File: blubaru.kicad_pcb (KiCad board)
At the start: 2 copper layers, 97.8 x 94.6 mm, 38 parts, among them J1 DB15, J2 DB15, J3 FSA2269, J4 ProMicro, J5 RN52_BREAKOUT, J6 JACK_TRS_6PINS, J7 TPA6112, P1 CONN_01X06, U1 DG419

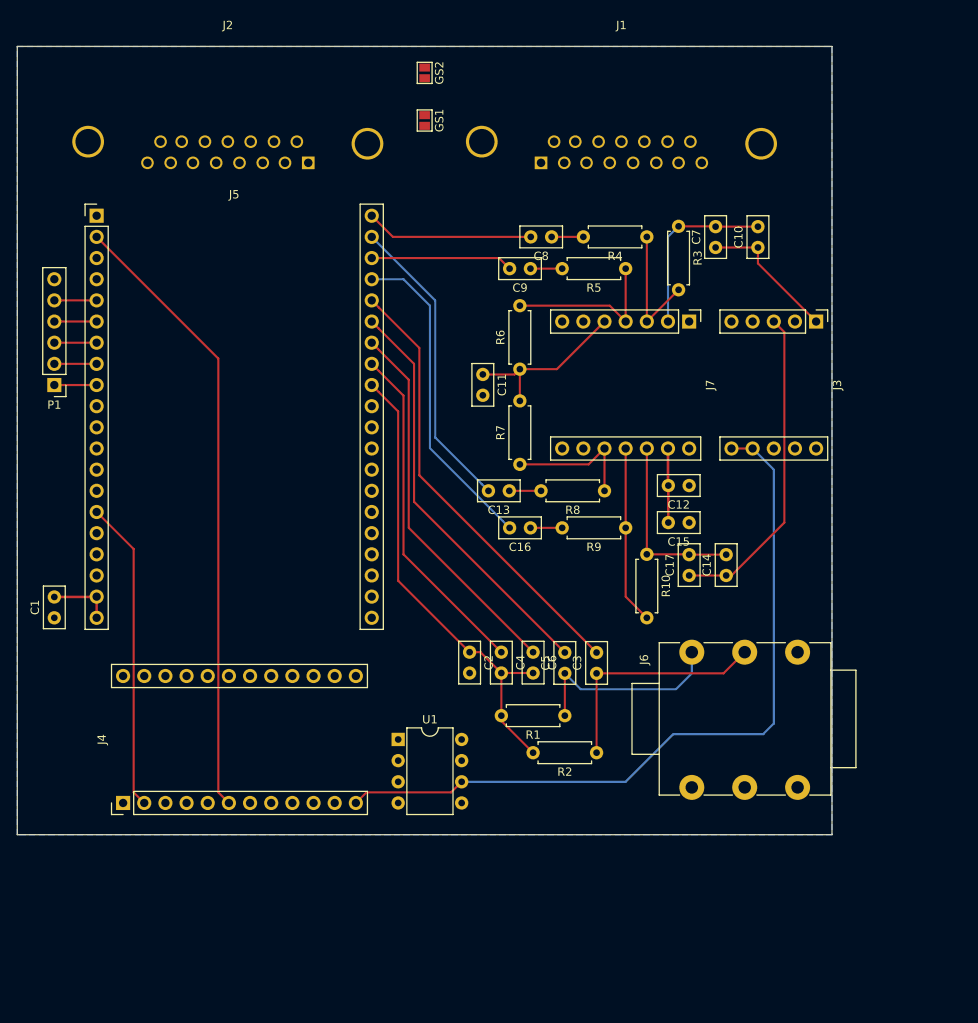
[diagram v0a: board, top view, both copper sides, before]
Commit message: Add footprints for LEDs and tactile switches
Also create an initial layout for fun.
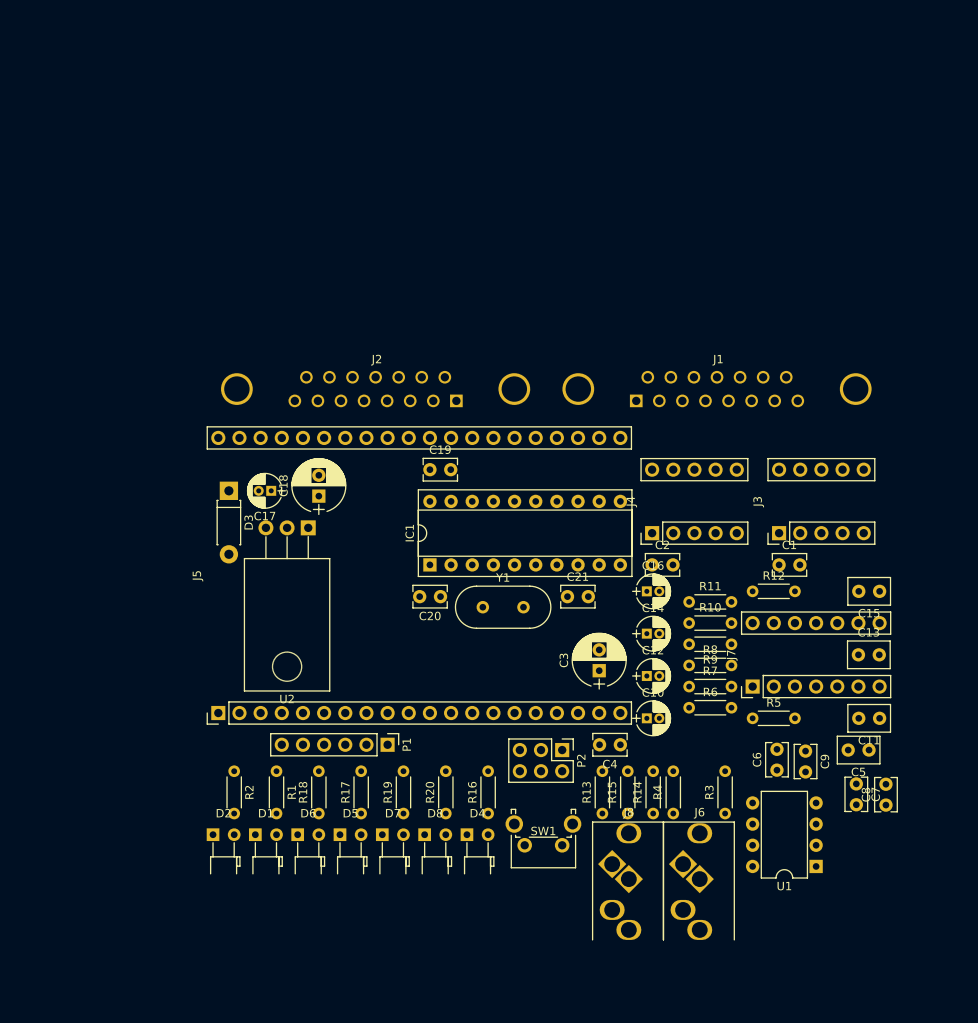
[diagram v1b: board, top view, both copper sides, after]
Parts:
- removed GS1, GS2: GS2, Connectors:GS2
- added C18: 100uF, blubaru:CP_Radial_D6.3mm_P2.50mm, F.Cu at (120.7, 83.8)
- added C19: 0.1uF, blubaru:C_Disc_D4.0mm_W2.6mm_P2.50mm, F.Cu at (134.0, 80.6)
- added C20: 22pF, blubaru:C_Disc_D4.0mm_W2.6mm_P2.50mm, F.Cu at (135.3, 95.9)
- added C21: 22pF, blubaru:C_Disc_D4.0mm_W2.6mm_P2.50mm, F.Cu at (150.5, 95.9)
- added D1: B LED, blubaru:LED_D3.0mm_Horizontal_O1.27mm_Z6.0mm, F.Cu at (113.0, 124.5)
- added D2: R LED, blubaru:LED_D3.0mm_Horizontal_O1.27mm_Z6.0mm, F.Cu at (108.0, 124.5)
- added D3: D, Diodes_THT:D_DO-41_SOD81_P7.62mm_Horizontal, F.Cu at (109.9, 83.2)
- added D4: R LED, blubaru:LED_D3.0mm_Horizontal_O1.27mm_Z6.0mm, F.Cu at (138.4, 124.5)
- added D5: O LED, blubaru:LED_D3.0mm_Horizontal_O1.27mm_Z6.0mm, F.Cu at (123.2, 124.5)
- added D6: Y LED, blubaru:LED_D3.0mm_Horizontal_O1.27mm_Z6.0mm, F.Cu at (118.1, 124.5)
- added D7: G LED, blubaru:LED_D3.0mm_Horizontal_O1.27mm_Z6.0mm, F.Cu at (128.3, 124.5)
- added D8: B LED, blubaru:LED_D3.0mm_Horizontal_O1.27mm_Z6.0mm, F.Cu at (133.3, 124.5)
- added IC1: ATTINY4313-P, Housings_DIP:DIP-20_W7.62mm_Socket, F.Cu at (134.0, 92.1)
- added J8: JACK_TRS_5PINS, blubaru:sj1-353xng, F.Cu at (157.9, 135.9)
- added P2: CONN_02X03, Pin_Headers:Pin_Header_Straight_2x03_Pitch2.54mm, F.Cu at (149.9, 114.3)
- added R11: 11k, Resistors_THT:R_Axial_DIN0204_L3.6mm_D1.6mm_P5.08mm_Horizontal, F.Cu at (165.1, 96.5)
- added R12: 8.2k, Resistors_THT:R_Axial_DIN0204_L3.6mm_D1.6mm_P5.08mm_Horizontal, F.Cu at (172.7, 95.2)
- added R13: 100k, Resistors_THT:R_Axial_DIN0204_L3.6mm_D1.6mm_P5.08mm_Horizontal, F.Cu at (154.7, 121.9)
- added R14: 100k, Resistors_THT:R_Axial_DIN0204_L3.6mm_D1.6mm_P5.08mm_Horizontal, F.Cu at (160.8, 121.9)
- added R15: 1M, Resistors_THT:R_Axial_DIN0204_L3.6mm_D1.6mm_P5.08mm_Horizontal, F.Cu at (157.7, 121.9)
- added R16: 750, Resistors_THT:R_Axial_DIN0204_L3.6mm_D1.6mm_P5.08mm_Horizontal, F.Cu at (141.0, 121.9)
- added R17: 750, Resistors_THT:R_Axial_DIN0204_L3.6mm_D1.6mm_P5.08mm_Horizontal, F.Cu at (125.7, 121.9)
- added R18: 750, Resistors_THT:R_Axial_DIN0204_L3.6mm_D1.6mm_P5.08mm_Horizontal, F.Cu at (120.7, 121.9)
- added R19: 330, Resistors_THT:R_Axial_DIN0204_L3.6mm_D1.6mm_P5.08mm_Horizontal, F.Cu at (130.8, 121.9)
- added R20: 330, Resistors_THT:R_Axial_DIN0204_L3.6mm_D1.6mm_P5.08mm_Horizontal, F.Cu at (135.9, 121.9)
- added SW1: SW_Push, blubaru:SW_Tactile_SPST_Angled_PTS645Vx58-2LFS, F.Cu at (149.9, 125.7)
- added U2: LD1117V33, TO_SOT_Packages_THT:TO-220_Horizontal, F.Cu at (119.4, 87.6)
- added Y1: 11.0592MHz, Crystals:Crystal_HC49-4H_Vertical, F.Cu at (140.3, 97.2)
- C1: footprint Capacitors_THT:C_Disc_D5.0mm_W2.5mm_P2.50mm -> blubaru:C_Disc_D4.0mm_W2.6mm_P2.50mm
- C10, C14: value 100uF -> 1uF; footprint Capacitors_THT:C_Disc_D5.0mm_W2.5mm_P2.50mm -> blubaru:CP_Radial_D4.0mm_P1.50mm
- C11, C13: footprint Capacitors_THT:C_Disc_D5.0mm_W2.5mm_P2.50mm -> blubaru:C_Disc_D5.0mm_W3.2mm_P2.50mm
- C12: value 0.1uF -> 1uF; footprint Capacitors_THT:C_Disc_D5.0mm_W2.5mm_P2.50mm -> blubaru:CP_Radial_D4.0mm_P1.50mm
- C15: value 10uF -> 1uF; footprint Capacitors_THT:C_Disc_D5.0mm_W2.5mm_P2.50mm -> blubaru:C_Disc_D5.0mm_W3.2mm_P2.50mm
- C16: footprint Capacitors_THT:C_Disc_D5.0mm_W2.5mm_P2.50mm -> blubaru:CP_Radial_D4.0mm_P1.50mm
- C17: value 100uF -> 10uF; footprint Capacitors_THT:C_Disc_D5.0mm_W2.5mm_P2.50mm -> blubaru:CP_Radial_D4.0mm_P1.50mm
- C2: value 1uF -> 0.1uF; footprint Capacitors_THT:C_Disc_D5.0mm_W2.5mm_P2.50mm -> blubaru:C_Disc_D4.0mm_W2.6mm_P2.50mm
- C3: value 47nF -> 220uF; footprint Capacitors_THT:C_Disc_D5.0mm_W2.5mm_P2.50mm -> blubaru:CP_Radial_D6.3mm_P2.50mm
- C4: value 47nF -> 0.1uF; footprint Capacitors_THT:C_Disc_D5.0mm_W2.5mm_P2.50mm -> blubaru:C_Disc_D4.0mm_W2.6mm_P2.50mm
- C5: value 47nF -> 1uF; footprint Capacitors_THT:C_Disc_D5.0mm_W2.5mm_P2.50mm -> blubaru:C_Disc_D5.0mm_W3.2mm_P2.50mm
- C6: value 47nF -> 0.047uF; footprint Capacitors_THT:C_Disc_D5.0mm_W2.5mm_P2.50mm -> blubaru:C_Disc_D4.0mm_W2.6mm_P2.50mm
- C7: value 100uF -> 0.047uF; footprint Capacitors_THT:C_Disc_D5.0mm_W2.5mm_P2.50mm -> blubaru:C_Disc_D4.0mm_W2.6mm_P2.50mm
- C8, C9: value 1uF -> 0.047uF; footprint Capacitors_THT:C_Disc_D5.0mm_W2.5mm_P2.50mm -> blubaru:C_Disc_D4.0mm_W2.6mm_P2.50mm
- J1: footprint Connectors:DB15FC -> blubaru:DB15FC
- J2: footprint Connectors:DB15MC -> blubaru:DB15MC
- J3: value FSA2269 -> TS5A22364-Q1; footprint blubaru:FSA2269 -> blubaru:TS5A22364-Q1
- J4: value ProMicro -> TS5A22364-Q1; footprint blubaru:ProMicro -> blubaru:TS5A22364-Q1
- J6: value JACK_TRS_6PINS -> JACK_TRS_5PINS; footprint Connectors:NMJ6HCD2 -> blubaru:sj1-353xng
- J7: value TPA6112 -> DRV632; footprint blubaru:TPA6112 -> blubaru:DRV632
- R1: value 2k2 -> 330; footprint Resistors_THT:R_Axial_DIN0207_L6.3mm_D2.5mm_P7.62mm_Horizontal -> Resistors_THT:R_Axial_DIN0204_L3.6mm_D1.6mm_P5.08mm_Horizontal
- R10, R6, R7: value 47k -> 11k; footprint Resistors_THT:R_Axial_DIN0207_L6.3mm_D2.5mm_P7.62mm_Horizontal -> Resistors_THT:R_Axial_DIN0204_L3.6mm_D1.6mm_P5.08mm_Horizontal
- R2: value 2k2 -> 750; footprint Resistors_THT:R_Axial_DIN0207_L6.3mm_D2.5mm_P7.62mm_Horizontal -> Resistors_THT:R_Axial_DIN0204_L3.6mm_D1.6mm_P5.08mm_Horizontal
- R3: value 47k -> 2k2; footprint Resistors_THT:R_Axial_DIN0207_L6.3mm_D2.5mm_P7.62mm_Horizontal -> Resistors_THT:R_Axial_DIN0204_L3.6mm_D1.6mm_P5.08mm_Horizontal
- R4: value 22k -> 2k2; footprint Resistors_THT:R_Axial_DIN0207_L6.3mm_D2.5mm_P7.62mm_Horizontal -> Resistors_THT:R_Axial_DIN0204_L3.6mm_D1.6mm_P5.08mm_Horizontal
- R5, R8, R9: value 22k -> 8.2k; footprint Resistors_THT:R_Axial_DIN0207_L6.3mm_D2.5mm_P7.62mm_Horizontal -> Resistors_THT:R_Axial_DIN0204_L3.6mm_D1.6mm_P5.08mm_Horizontal
- moved C1 87.2 mm to (175.9, 92.1), turned to 0 degrees
- moved C8 79.1 mm to (188.7, 120.9), turned to 90 degrees
- moved R3 70.7 mm to (169.4, 121.9), turned to 90 degrees
- moved J4 69.6 mm to (160.7, 84.5)
- moved R4 69.3 mm to (163.2, 121.9), turned to 90 degrees
- moved C9 66.7 mm to (179.1, 114.4), turned to 270 degrees
- moved C7 66.6 mm to (185.2, 118.4), turned to 270 degrees
- moved C11 63.0 mm to (188.0, 110.5), turned to 180 degrees
- moved P1 58.9 mm to (128.9, 113.7), turned to 270 degrees
- moved C10 58.1 mm to (160.0, 110.5), turned to 0 degrees
- moved R5 56.1 mm to (172.7, 110.5), turned to 0 degrees
- moved U1 52.4 mm to (180.3, 128.3), turned to 180 degrees
- moved C17 51.2 mm to (114.9, 83.2), turned to 180 degrees
- moved C13 46.3 mm to (185.4, 102.9), turned to 0 degrees
- moved R6 45.4 mm to (165.1, 109.2), turned to 0 degrees
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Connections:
- C1 pad 1: GND -> VCC
- C1 pad 2: VCC -> GND
- C10 pad 1: /DB-15 interconnects/Modules/Audio switch/BT_L -> /DB-15 interconnects/Modules/Bluetooth Module/Line Driver/R-
- C12 pad 1: GND -> /DB-15 interconnects/Modules/Bluetooth Module/Line Driver/R+
- C12 pad 2: VCC -> Net-(C12-Pad2)
- C13 pad 2: /DB-15 interconnects/Modules/Bluetooth Module/Amp/R+ -> Net-(C13-Pad2)
- C14 pad 1: /DB-15 interconnects/Modules/Audio switch/BT_R -> /DB-15 interconnects/Modules/Bluetooth Module/Line Driver/L+
- C15 pad 1: GND -> VCC
- C15 pad 2: VCC -> GND
- C16 pad 1: Net-(C16-Pad1) -> /DB-15 interconnects/Modules/Bluetooth Module/Line Driver/L-
- C16 pad 2: /DB-15 interconnects/Modules/Bluetooth Module/Amp/R- -> Net-(C16-Pad2)
- C17 pad 1: /DB-15 interconnects/Modules/Audio switch/BT_R -> Net-(C17-Pad1)
- C17 pad 2: Net-(C14-Pad2) -> GND
- C2 pad 1: /DB-15 interconnects/Modules/Bluetooth Module/Microphone/MIC_BIAS -> VCC
- C3 pad 1: Net-(C3-Pad1) -> VCC
- C3 pad 2: /DB-15 interconnects/Modules/Bluetooth Module/Microphone/MIC_R- -> GND
- C4 pad 1: /DB-15 interconnects/Modules/Bluetooth Module/Microphone/MIC_L+ -> VCC
- C4 pad 2: /DB-15 interconnects/Modules/Bluetooth Module/Microphone/MIC_BIAS -> GND
- C5 pad 1: Net-(C5-Pad1) -> /DB-15 interconnects/Modules/Bluetooth Module/Microphone/MIC_BIAS
- C5 pad 2: /DB-15 interconnects/Modules/Bluetooth Module/Microphone/MIC_L- -> GND
- C6 pad 1: /DB-15 interconnects/Modules/Bluetooth Module/Microphone/MIC_R+ -> Net-(C6-Pad1)
- C6 pad 2: /DB-15 interconnects/Modules/Bluetooth Module/Microphone/MIC_BIAS -> /DB-15 interconnects/Modules/Bluetooth Module/Microphone/MIC_R-
- C7 pad 1: /DB-15 interconnects/Modules/Audio switch/BT_L -> /DB-15 interconnects/Modules/Bluetooth Module/Microphone/MIC_L+
- C7 pad 2: Net-(C10-Pad2) -> /DB-15 interconnects/Modules/Bluetooth Module/Microphone/MIC_BIAS
- C8 pad 2: /DB-15 interconnects/Modules/Bluetooth Module/Amp/L+ -> /DB-15 interconnects/Modules/Bluetooth Module/Microphone/MIC_L-
- C9 pad 1: Net-(C9-Pad1) -> /DB-15 interconnects/Modules/Bluetooth Module/Microphone/MIC_R+
- C9 pad 2: /DB-15 interconnects/Modules/Bluetooth Module/Amp/L- -> /DB-15 interconnects/Modules/Bluetooth Module/Microphone/MIC_BIAS
- J1 pad 15: Net-(J1-Pad15) -> (no net)
- J2 pad 15: Net-(J2-Pad15) -> (no net)
- J3 pad 1: /DB-15 interconnects/Modules/Audio switch/BT_L -> VCC
- J3 pad 10: /DB-15 interconnects/4_IN -> /DB-15 interconnects/Modules/Audio switch/LINE_R
- J3 pad 2: /DB-15 interconnects/2_IN -> /DB-15 interconnects/Modules/Audio switch/LINE_L
- J3 pad 3: /DB-15 interconnects/Modules/Audio switch/BT_R -> Net-(J3-Pad3)
- J3 pad 4: GND -> /DB-15 interconnects/Modules/Audio switch/BT_L
- J3 pad 5: /DB-15 interconnects/2_OUT -> /DB-15 interconnects/Modules/Audio switch/LINE_TRG
- J3 pad 6: /DB-15 interconnects/Modules/Audio switch/BT_TRG -> GND
- J3 pad 7: /DB-15 interconnects/Modules/Audio switch/BT_TRG -> /DB-15 interconnects/Modules/Audio switch/LINE_TRG
- J3 pad 8: /DB-15 interconnects/4_OUT -> /DB-15 interconnects/Modules/Audio switch/BT_R
- J3 pad 9: VCC -> Net-(J3-Pad9)
- J4 pad 1: /DB-15 interconnects/Modules/Bluetooth Module/UART_RX -> VCC
- J4 pad 10: Net-(J4-Pad10) -> Net-(J3-Pad9)
- J4 pad 2: /DB-15 interconnects/Modules/Bluetooth Module/UART_TX -> Net-(J3-Pad3)
- J4 pad 3: GND -> /DB-15 interconnects/4_OUT
- J4 pad 4: GND -> /DB-15 interconnects/4_IN
- J4 pad 5: /DB-15 interconnects/Modules/Bluetooth Module/CMD -> /DB-15 interconnects/Modules/Audio switch/BT_TRG
- J4 pad 6: /DB-15 interconnects/Modules/Bluetooth Module/EVENT -> GND
- J4 pad 7: Net-(J4-Pad7) -> /DB-15 interconnects/Modules/Audio switch/BT_TRG
- J4 pad 8: Net-(J4-Pad8) -> /DB-15 interconnects/2_IN
- J4 pad 9: Net-(J4-Pad9) -> /DB-15 interconnects/2_OUT
- J5 pad 1: Net-(J5-Pad1) -> /DB-15 interconnects/Modules/Bluetooth Module/RESET
- J5 pad 11: Net-(J5-Pad11) -> (no net)
- J5 pad 12: Net-(J5-Pad12) -> (no net)
- J5 pad 13: Net-(J5-Pad13) -> (no net)
- J5 pad 14: Net-(J5-Pad14) -> (no net)
- J5 pad 17: Net-(J5-Pad17) -> /DB-15 interconnects/Modules/Bluetooth Module/9600
- J5 pad 18: Net-(J5-Pad18) -> (no net)
- J5 pad 19: VCC -> /DB-15 interconnects/Modules/Bluetooth Module/PWR_EN
- J5 pad 22: Net-(J5-Pad22) -> (no net)
- J5 pad 23: Net-(J5-Pad23) -> (no net)
- J5 pad 24: Net-(J5-Pad24) -> (no net)
- J5 pad 25: Net-(J5-Pad25) -> (no net)
- J5 pad 26: Net-(J5-Pad26) -> (no net)
- J5 pad 27: Net-(J5-Pad27) -> (no net)
- J5 pad 28: Net-(J5-Pad28) -> (no net)
- J5 pad 29: Net-(J5-Pad29) -> (no net)
- J5 pad 3: Net-(J5-Pad3) -> (no net)
- J5 pad 37: /DB-15 interconnects/Modules/Bluetooth Module/Amp/R- -> /DB-15 interconnects/Modules/Bluetooth Module/Line Driver/R-
- J5 pad 38: /DB-15 interconnects/Modules/Bluetooth Module/Amp/L- -> /DB-15 interconnects/Modules/Bluetooth Module/Line Driver/L-
- J5 pad 39: /DB-15 interconnects/Modules/Bluetooth Module/Amp/R+ -> /DB-15 interconnects/Modules/Bluetooth Module/Line Driver/R+
- J5 pad 4: Net-(J5-Pad4) -> (no net)
- J5 pad 40: /DB-15 interconnects/Modules/Bluetooth Module/Amp/L+ -> /DB-15 interconnects/Modules/Bluetooth Module/Line Driver/L+
- J6 pad 2: Net-(C5-Pad1) -> Net-(C8-Pad1)
- J6 pad 3: Net-(C3-Pad1) -> Net-(C6-Pad1)
- J6 pad 4: Net-(J6-Pad4) -> (no net)
- J6 pad 5: Net-(J6-Pad5) -> (no net)
- J7 pad 1: GND -> Net-(J7-Pad1)
- J7 pad 10: Net-(J7-Pad10) -> GND
- J7 pad 11: Net-(J7-Pad11) -> (no net)
- J7 pad 12: Net-(C14-Pad2) -> /DB-15 interconnects/Modules/Audio switch/BT_R
- J7 pad 13: VCC -> Net-(J7-Pad13)
- J7 pad 14: GND -> Net-(J7-Pad14)
- J7 pad 2: Net-(C10-Pad2) -> Net-(J7-Pad2)
- J7 pad 3: Net-(J7-Pad3) -> /DB-15 interconnects/Modules/Audio switch/BT_L
- J7 pad 4: Net-(J7-Pad4) -> GND
- J7 pad 5: Net-(C11-Pad1) -> VCC
- J7 pad 6: GND -> Net-(C11-Pad1)
- J7 pad 7: GND -> Net-(C13-Pad2)
- J7 pad 8: GND -> Net-(C13-Pad1)
- J7 pad 9: GND -> VCC
- R1 pad 1: Net-(C5-Pad1) -> VCC
- R1 pad 2: /DB-15 interconnects/Modules/Bluetooth Module/Microphone/MIC_BIAS -> Net-(D1-Pad2)
- R10 pad 2: Net-(J7-Pad11) -> Net-(J7-Pad14)
- R2 pad 1: Net-(C3-Pad1) -> VCC
- R2 pad 2: /DB-15 interconnects/Modules/Bluetooth Module/Microphone/MIC_BIAS -> Net-(D2-Pad2)
- R3 pad 1: Net-(C10-Pad2) -> Net-(C8-Pad1)
- R3 pad 2: Net-(J7-Pad3) -> /DB-15 interconnects/Modules/Bluetooth Module/Microphone/MIC_BIAS
- R4 pad 1: Net-(J7-Pad3) -> Net-(C6-Pad1)
- R4 pad 2: Net-(C8-Pad1) -> /DB-15 interconnects/Modules/Bluetooth Module/Microphone/MIC_BIAS
- R5 pad 1: Net-(J7-Pad4) -> Net-(J7-Pad2)
- R5 pad 2: Net-(C9-Pad1) -> /DB-15 interconnects/Modules/Audio switch/BT_L
- R6 pad 1: Net-(C11-Pad1) -> Net-(C10-Pad2)
- R6 pad 2: Net-(J7-Pad4) -> Net-(J7-Pad2)
- R7 pad 1: Net-(J7-Pad10) -> Net-(C12-Pad2)
- R7 pad 2: Net-(C11-Pad1) -> Net-(J7-Pad1)
- R8 pad 1: Net-(J7-Pad10) -> GNDA
- R8 pad 2: Net-(C13-Pad1) -> Net-(J7-Pad1)
- R9 pad 1: Net-(J7-Pad11) -> Net-(J7-Pad14)
- R9 pad 2: Net-(C16-Pad1) -> GNDA
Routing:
- net /DB-15 interconnects/Modules/Audio switch/BT_TRG: track 90.7 -> 0.00 mm
- net /DB-15 interconnects/Modules/Bluetooth Module/EVENT: track 74.5 -> 0.00 mm
- net /DB-15 interconnects/Modules/Bluetooth Module/Microphone/MIC_BIAS: track 56.7 -> 0.00 mm
- net /DB-15 interconnects/Modules/Bluetooth Module/Microphone/MIC_R-: track 53.4 -> 0.00 mm
- net /DB-15 interconnects/Modules/Bluetooth Module/Microphone/MIC_L-: track 49.3 -> 0.00 mm
- net /DB-15 interconnects/Modules/Bluetooth Module/Microphone/MIC_R+: track 45.2 -> 0.00 mm
- net /DB-15 interconnects/Modules/Bluetooth Module/Microphone/MIC_L+: track 41.1 -> 0.00 mm
- net /DB-15 interconnects/Modules/Bluetooth Module/Amp/R-: track 38.9 -> 0.00 mm
- net /DB-15 interconnects/Modules/Audio switch/BT_R: track 38.7 -> 0.00 mm
- net /DB-15 interconnects/Modules/Bluetooth Module/UART_TX: track 37.3 -> 0.00 mm
- net /DB-15 interconnects/Modules/Bluetooth Module/Amp/R+: track 36.9 -> 0.00 mm
- net Net-(C3-Pad1): track 28.4 -> 0.00 mm
- net Net-(C5-Pad1): track 24.4 -> 0.00 mm
- net Net-(C14-Pad2): track 22.2 -> 0.00 mm
- net Net-(C10-Pad2): track 21.5 -> 0.00 mm
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- removed copper zone on B.Cu, net GND
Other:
- board outline removed
